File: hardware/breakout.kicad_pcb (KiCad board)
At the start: 2 copper layers, 40.3 x 50 mm, 8 parts, among them J1 Conn_01x18_Male, J2 Conn_Coaxial, J3 Conn_01x18_Male, J4 Conn_Coaxial, SW1 SW_Push, U1 RFM95W-915S2

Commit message: [add] Debouncing circuit
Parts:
- added C2: 1uF, Capacitor_SMD:C_1206_3216Metric_Pad1.33x1.80mm_HandSolder, F.Cu at (145.2, 95.2)
- added R1: 220R, Resistor_SMD:R_1206_3216Metric_Pad1.30x1.75mm_HandSolder, F.Cu at (145.2, 97.8)
- added R2: 10KR, Resistor_SMD:R_1206_3216Metric_Pad1.30x1.75mm_HandSolder, F.Cu at (145.2, 85.1)
- C1: value C_Small -> 10uF
- moved SW1 2.75 mm to (145.3, 90.8)
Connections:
- J3 pad 16: /RST -> /RST_GPIO
- SW1 pad 2: /RST -> /RST_GPIO
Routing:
- net /RST_GPIO: track 0.00 -> 37.4 mm
- net +3V3: track 31.0 -> 63.5 mm, vias 2 -> 3
- net /RST: track 46.5 -> 21.5 mm, vias 1 -> 0

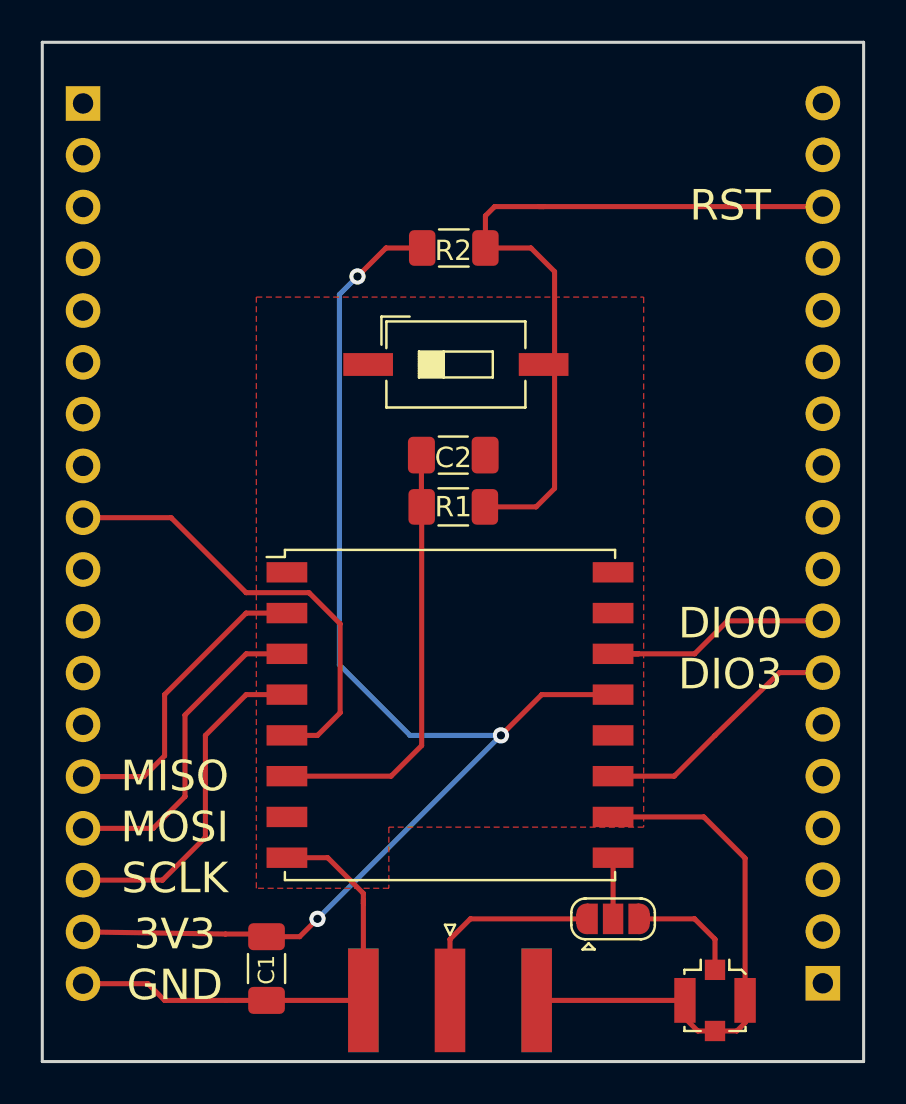
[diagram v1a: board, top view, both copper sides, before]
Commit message: [fix] fixed board size + 3v3 input + reset button
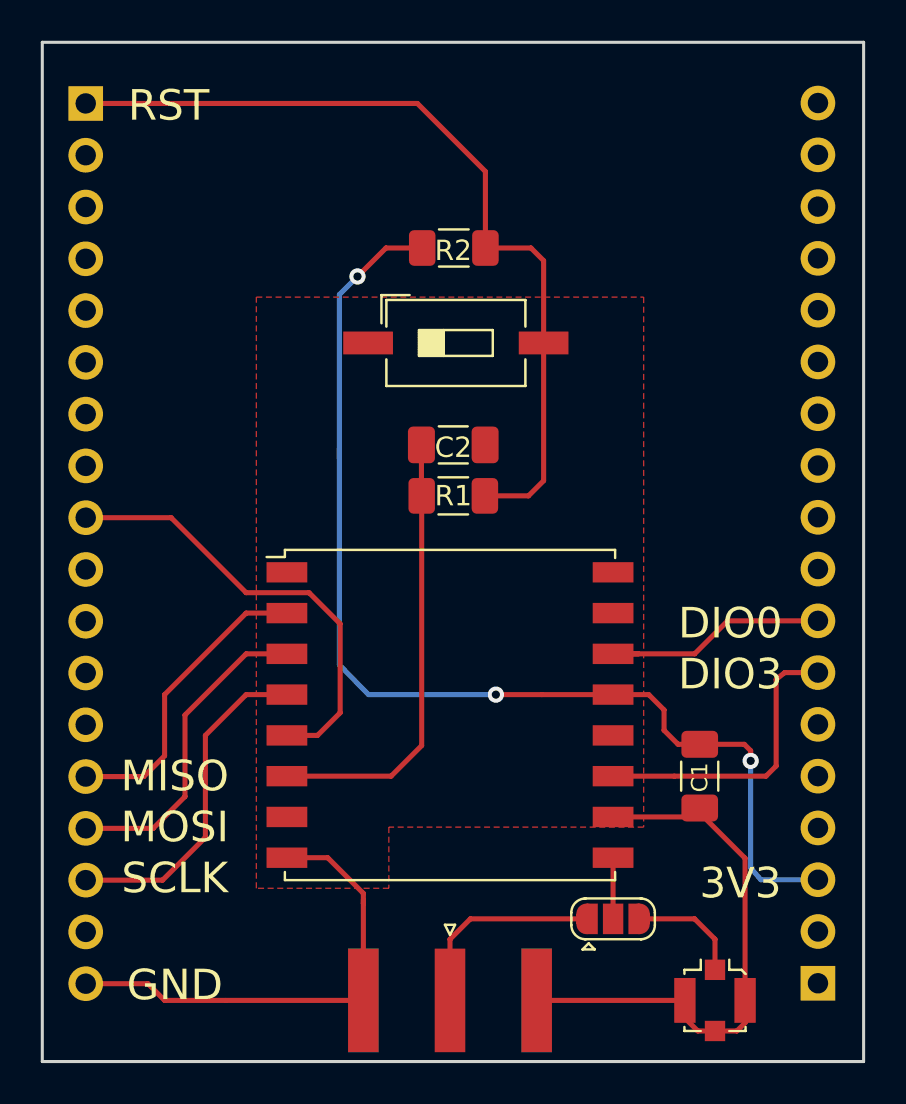
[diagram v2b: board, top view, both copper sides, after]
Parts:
- moved C1 23.3 mm to (157.2, 111.0)
- moved SW1 1.06 mm to (145.3, 89.8)
- moved R1 0.54 mm to (145.2, 97.2)
- moved C2 0.50 mm to (145.2, 94.8)
- moved J3 0.24 mm to (163.1, 121.2)
- moved J1 0.13 mm to (127.1, 78.0)
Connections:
- J1 pad 1: Net-(J1-Pad1) -> /RST_GPIO
- J1 pad 10: Net-(J1-Pad10) -> (no net)
- J1 pad 11: Net-(J1-Pad11) -> (no net)
- J1 pad 12: Net-(J1-Pad12) -> (no net)
- J1 pad 13: Net-(J1-Pad13) -> (no net)
- J1 pad 17: +3V3 -> (no net)
- J1 pad 2: Net-(J1-Pad2) -> (no net)
- J1 pad 3: Net-(J1-Pad3) -> (no net)
- J1 pad 4: Net-(J1-Pad4) -> (no net)
- J1 pad 5: Net-(J1-Pad5) -> (no net)
- J1 pad 6: Net-(J1-Pad6) -> (no net)
- J1 pad 7: Net-(J1-Pad7) -> (no net)
- J1 pad 8: Net-(J1-Pad8) -> (no net)
- J3 pad 1: Net-(J3-Pad1) -> (no net)
- J3 pad 10: Net-(J3-Pad10) -> (no net)
- J3 pad 11: Net-(J3-Pad11) -> (no net)
- J3 pad 12: Net-(J3-Pad12) -> (no net)
- J3 pad 13: Net-(J3-Pad13) -> (no net)
- J3 pad 14: Net-(J3-Pad14) -> (no net)
- J3 pad 15: Net-(J3-Pad15) -> (no net)
- J3 pad 16: /RST_GPIO -> (no net)
- J3 pad 17: Net-(J3-Pad17) -> (no net)
- J3 pad 18: Net-(J3-Pad18) -> (no net)
- J3 pad 2: Net-(J3-Pad2) -> (no net)
- J3 pad 3: Net-(J3-Pad3) -> +3V3
- J3 pad 4: Net-(J3-Pad4) -> (no net)
- J3 pad 5: Net-(J3-Pad5) -> (no net)
- J3 pad 6: Net-(J3-Pad6) -> (no net)
- J3 pad 9: Net-(J3-Pad9) -> (no net)
- U1 pad 12: Net-(U1-Pad12) -> (no net)
- U1 pad 15: Net-(U1-Pad15) -> (no net)
- U1 pad 16: Net-(U1-Pad16) -> (no net)
- U1 pad 7: Net-(U1-Pad7) -> (no net)
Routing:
- net +3V3: track 63.5 -> 55.7 mm
- net /RST_GPIO: track 37.4 -> 41.8 mm
- net /DIO3: track 12.1 -> 14.6 mm
- net /RST: track 21.5 -> 22.7 mm
